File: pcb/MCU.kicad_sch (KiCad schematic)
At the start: 1 part, among them U1 WeMos_S2_mini

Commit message: added VR input IC conditioner
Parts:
- U1: footprint Module:WEMOS_S2_mini -> MCU_Custom:WEMOS_S2_mini
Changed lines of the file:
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@@
 			)
 		)
-		(property "Footprint" "Module:WEMOS_S2_mini"
+		(property "Footprint" "MCU_Custom:WEMOS_S2_mini"
 			(at 160.02 127 0)
 			(effects

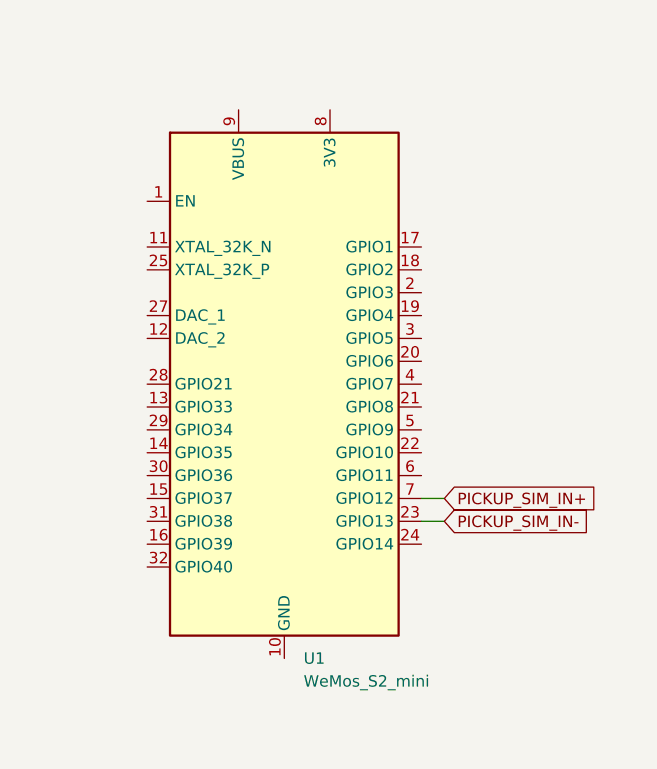
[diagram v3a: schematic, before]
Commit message: added SSR
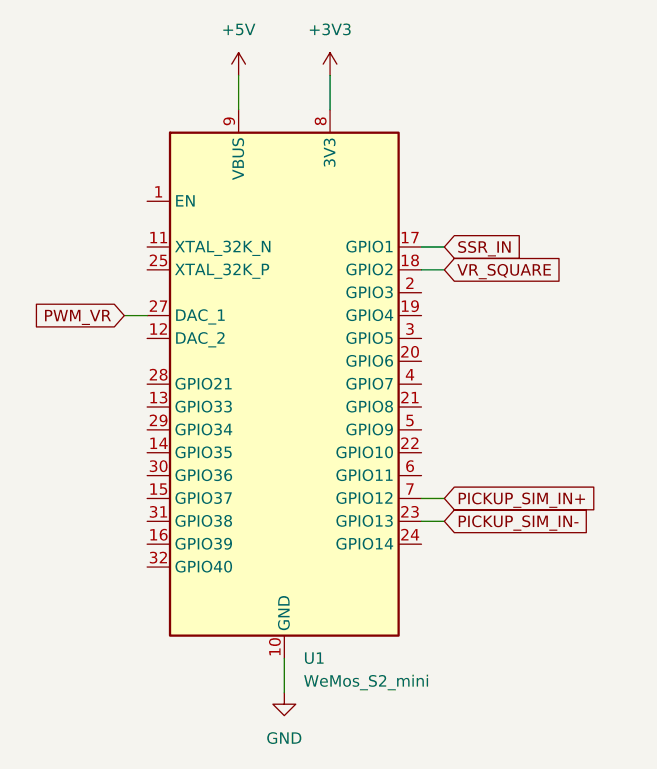
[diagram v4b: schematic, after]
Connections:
- net GND: now reaches U1.10 (GND), U1.26 (GND)
- net SSR_IN: now reaches U1.17 (GPIO1)
- net VR_SQUARE: now reaches U1.18 (GPIO2)
- net PWM_VR: now reaches U1.27 (DAC_1)
- net +3V3: now reaches U1.8 (3V3)
- net +5V: now reaches U1.9 (VBUS)

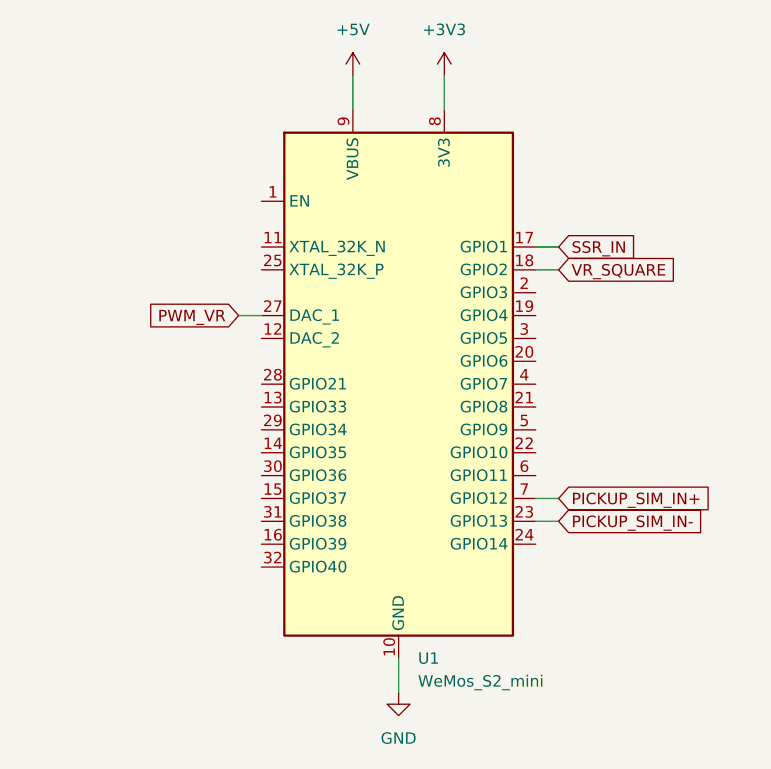
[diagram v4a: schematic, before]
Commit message: added batteryless function
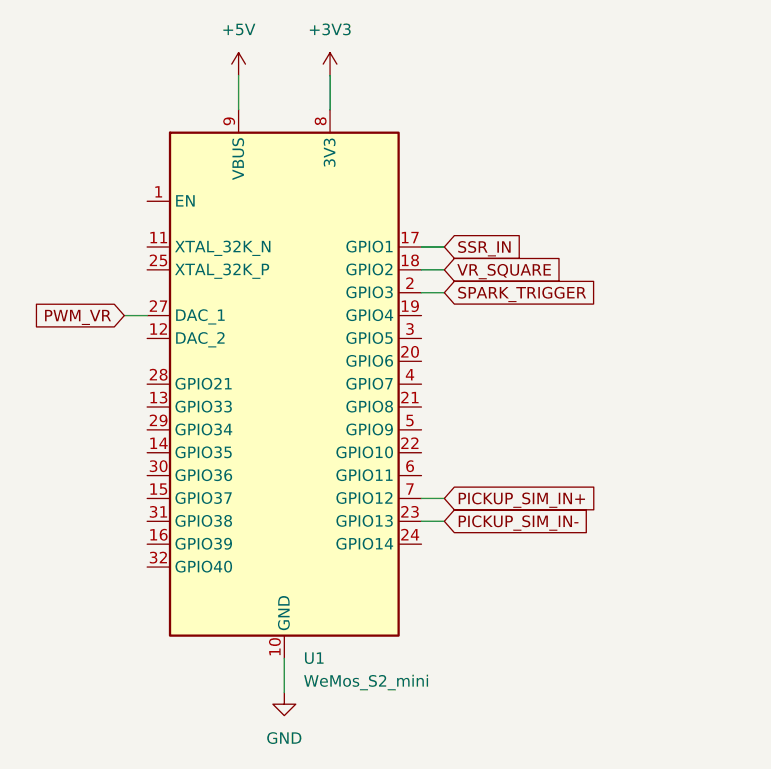
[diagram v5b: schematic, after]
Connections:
- net SPARK_TRIGGER: now reaches U1.2 (GPIO3)
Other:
- moved on the sheet: U1
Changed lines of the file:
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@@
 	(wire
 		(pts
-			(xy 154.94 46.99) (xy 154.94 50.8)
-		)
-		(stroke
-			(width 0)
-			(type default)
-		)
-	)
-	(wire
-		(pts
-			(xy 177.8 66.04) (xy 175.26 66.04)
-		)
-		(stroke
-			(width 0)
-			(type default)
-		)
-	)
-	(wire
-		(pts
-			(xy 160.02 115.57) (xy 160.02 111.76)
-		)
-		(stroke
-			(width 0)
-			(type default)
-		)
-	)
-	(wire
-		(pts
-			(xy 177.8 68.58) (xy 175.26 68.58)
-		)
-		(stroke
-			(width 0)
-			(type default)
-		)
-	)
-	(wire
-		(pts
-			(xy 165.1 46.99) (xy 165.1 50.8)
-		)
-		(stroke
-			(width 0)
-			(type default)
-		)
-	)
-	(wire
-		(pts
-			(xy 177.8 96.52) (xy 175.26 96.52)
-		)
-		(stroke
-			(width 0)
-			(type default)
-		)
-	)
-	(wire
-		(pts
-			(xy 177.8 93.98) (xy 175.26 93.98)
-		)
-		(stroke
-			(width 0)
-			(type default)
-		)
-	)
-	(wire
-		(pts
-			(xy 142.24 73.66) (xy 144.78 73.66)
-		)
-		(stroke
-			(width 0)
-			(type default)
-		)
-	)
-	(global_label "VR_SQUARE"
+			(xy 142.24 46.99) (xy 142.24 50.8)
+		)
+		(stroke
+			(width 0)
+			(type default)
+		)
+	)
+	(wire
+		(pts
+			(xy 165.1 71.12) (xy 162.56 71.12)
+		)
+		(stroke
+			(width 0)
+			(type default)
+		)
+	)
+	(wire
+		(pts
+			(xy 165.1 66.04) (xy 162.56 66.04)
+		)
+		(stroke
+			(width 0)
+			(type default)
+		)
+	)
+	(wire
+		(pts
+			(xy 147.32 115.57) (xy 147.32 111.76)
+		)
+		(stroke
+			(width 0)
+			(type default)
+		)
+	)
+	(wire
+		(pts
+			(xy 165.1 68.58) (xy 162.56 68.58)
+		)
+		(stroke
+			(width 0)
+			(type default)
+		)
+	)
+	(wire
+		(pts
+			(xy 152.4 46.99) (xy 152.4 50.8)
+		)
+		(stroke
+			(width 0)
+			(type default)
+		)
+	)
+	(wire
+		(pts
+			(xy 165.1 96.52) (xy 162.56 96.52)
+		)
+		(stroke
+			(width 0)
+			(type default)
+		)
+	)
+	(wire
+		(pts
+			(xy 165.1 93.98) (xy 162.56 93.98)
+		)
+		(stroke
+			(width 0)
+			(type default)
+		)
+	)
+	(wire
+		(pts
+			(xy 129.54 73.66) (xy 132.08 73.66)
+		)
+		(stroke
+			(width 0)
+			(type default)
+		)
+	)
+	(global_label "SPARK_TRIGGER"
 		(shape input)
-		(at 177.8 68.58 0)
+		(at 165.1 71.12 0)
 		(fields_autoplaced yes)
 		(effects
@@
 		)
 		(property "Intersheetrefs" "${INTERSHEET_REFS}"
-			(at 191.4895 68.58 0)
-			(effects
-				(font
-					(size 1.27 1.27)
-				)
-				(justify left)
-				(hide yes)
-			)
-		)
-	)
-	(global_label "PICKUP_SIM_IN+"
+			(at 182.9623 71.12 0)
+			(effects
+				(font
+					(size 1.27 1.27)
+				)
+				(justify left)
+				(hide yes)
+			)
+		)
+	)
+	(global_label "VR_SQUARE"
 		(shape input)
-		(at 177.8 93.98 0)
+		(at 165.1 68.58 0)
 		(fields_autoplaced yes)
 		(effects
@@
 		)
 		(property "Intersheetrefs" "${INTERSHEET_REFS}"
-			(at 196.5091 93.98 0)
-			(effects
-				(font
-					(size 1.27 1.27)
-				)
-				(justify left)
-				(hide yes)
-			)
-		)
-	)
-	(global_label "PICKUP_SIM_IN-"
+			(at 178.7895 68.58 0)
+			(effects
+				(font
+					(size 1.27 1.27)
+				)
+				(justify left)
+				(hide yes)
+			)
+		)
+	)
+	(global_label "PICKUP_SIM_IN+"
 		(shape input)
-		(at 177.8 96.52 0)
+		(at 165.1 93.98 0)
 		(fields_autoplaced yes)
 		(effects
@@
 		)
 		(property "Intersheetrefs" "${INTERSHEET_REFS}"
-			(at 196.5091 96.52 0)
-			(effects
-				(font
-					(size 1.27 1.27)
-				)
-				(justify left)
-				(hide yes)
-			)
-		)
-	)
-	(global_label "SSR_IN"
+			(at 183.8091 93.98 0)
+			(effects
+				(font
+					(size 1.27 1.27)
+				)
+				(justify left)
+				(hide yes)
+			)
+		)
+	)
+	(global_label "PICKUP_SIM_IN-"
 		(shape input)
-		(at 177.8 66.04 0)
+		(at 165.1 96.52 0)
 		(fields_autoplaced yes)
 		(effects
@@
 		)
 		(property "Intersheetrefs" "${INTERSHEET_REFS}"
-			(at 187.3771 66.04 0)
-			(effects
-				(font
-					(size 1.27 1.27)
-				)
-				(justify left)
-				(hide yes)
-			)
-		)
-	)
-	(global_label "PWM_VR"
+			(at 183.8091 96.52 0)
+			(effects
+				(font
+					(size 1.27 1.27)
+				)
+				(justify left)
+				(hide yes)
+			)
+		)
+	)
+	(global_label "SSR_IN"
 		(shape input)
-		(at 142.24 73.66 180)
+		(at 165.1 66.04 0)
 		(fields_autoplaced yes)
 		(effects
@@
 				(size 1.27 1.27)
 			)
+			(justify left)
+		)
+		(property "Intersheetrefs" "${INTERSHEET_REFS}"
+			(at 174.6771 66.04 0)
+			(effects
+				(font
+					(size 1.27 1.27)
+				)
+				(justify left)
+				(hide yes)
+			)
+		)
+	)
+	(global_label "PWM_VR"
+		(shape input)
+		(at 129.54 73.66 180)
+		(fields_autoplaced yes)
+		(effects
+			(font
+				(size 1.27 1.27)
+			)
 			(justify right)
 		)
 		(property "Intersheetrefs" "${INTERSHEET_REFS}"
-			(at 131.7558 73.66 0)
+			(at 119.0558 73.66 0)
 			(effects
 				(font
@@
 	(symbol
 		(lib_id "power:+5V")
-		(at 154.94 46.99 0)
+		(at 142.24 46.99 0)
 		(unit 1)
 		(exclude_from_sim no)
@@
 		(fields_autoplaced yes)
 		(property "Reference" "#PWR08"
-			(at 154.94 50.8 0)
+			(at 142.24 50.8 0)
 			(effects
 				(font
@@
 		)
 		(property "Value" "+5V"
-			(at 154.94 41.91 0)
+			(at 142.24 41.91 0)
 			(effects
 				(font
@@
 		)
 		(property "Footprint" ""
-			(at 154.94 46.99 0)
+			(at 142.24 46.99 0)
 			(effects
 				(font
@@
 		)
 		(property "Datasheet" ""
-			(at 154.94 46.99 0)
+			(at 142.24 46.99 0)
 			(effects
 				(font
@@
 		)
 		(property "Description" "Power symbol creates a global label with name \"+5V\""
-			(at 154.94 46.99 0)
+			(at 142.24 46.99 0)
 			(effects
 				(font
@@
 	(symbol
 		(lib_id "power:+3V3")
-		(at 165.1 46.99 0)
+		(at 152.4 46.99 0)
 		(unit 1)
 		(exclude_from_sim no)
@@
 		(fields_autoplaced yes)
 		(property "Reference" "#PWR07"
-			(at 165.1 50.8 0)
+			(at 152.4 50.8 0)
 			(effects
 				(font
@@
 		)
 		(property "Value" "+3V3"
-			(at 165.1 41.91 0)
+			(at 152.4 41.91 0)
 			(effects
 				(font
@@
 		)
 		(property "Footprint" ""
-			(at 165.1 46.99 0)
+			(at 152.4 46.99 0)
 			(effects
 				(font
@@
 		)
 		(property "Datasheet" ""
-			(at 165.1 46.99 0)
+			(at 152.4 46.99 0)
 			(effects
 				(font
@@
 		)
 		(property "Description" "Power symbol creates a global label with name \"+3V3\""
-			(at 165.1 46.99 0)
+			(at 152.4 46.99 0)
 			(effects
 				(font
@@
 	(symbol
 		(lib_id "MCU_Custom:WeMos_S2_mini")
-		(at 160.02 81.28 0)
+		(at 147.32 81.28 0)
 		(unit 1)
 		(exclude_from_sim no)
@@
 		(fields_autoplaced yes)
 		(property "Reference" "U1"
-			(at 162.1633 111.76 0)
+			(at 149.4633 111.76 0)
 			(effects
 				(font
@@
 		)
 		(property "Value" "WeMos_S2_mini"
-			(at 162.1633 114.3 0)
+			(at 149.4633 114.3 0)
 			(effects
 				(font
@@
 		)
 		(property "Footprint" "MCU_Custom:WEMOS_S2_mini"
-			(at 160.02 127 0)
+			(at 147.32 127 0)
 			(effects
 				(font
@@
 		)
 		(property "Datasheet" "https://www.wemos.cc/en/latest/s2/s2_mini.html"
-			(at 160.02 124.46 0)
+			(at 147.32 124.46 0)
 			(effects
 				(font
@@
 		)
 		(property "Description" "32-bit microcontroller module with WiFi"
-			(at 160.02 81.28 0)
+			(at 147.32 81.28 0)
 			(effects
 				(font
@@
 	(symbol
 		(lib_id "power:GND")
-		(at 160.02 115.57 0)
+		(at 147.32 115.57 0)
 		(unit 1)
 		(exclude_from_sim no)
@@
 		(fields_autoplaced yes)
 		(property "Reference" "#PWR06"
-			(at 160.02 121.92 0)
+			(at 147.32 121.92 0)
 			(effects
 				(font
@@
 		)
 		(property "Value" "GND"
-			(at 160.02 120.65 0)
+			(at 147.32 120.65 0)
 			(effects
 				(font
@@
 		)
 		(property "Footprint" ""
-			(at 160.02 115.57 0)
+			(at 147.32 115.57 0)
 			(effects
 				(font
@@
 		)
 		(property "Datasheet" ""
-			(at 160.02 115.57 0)
+			(at 147.32 115.57 0)
 			(effects
 				(font
@@
 		)
 		(property "Description" "Power symbol creates a global label with name \"GND\" , ground"
-			(at 160.02 115.57 0)
-			(effects
-				(font
+			(at 147.32 115.57 0)
+			(effects
+				(font

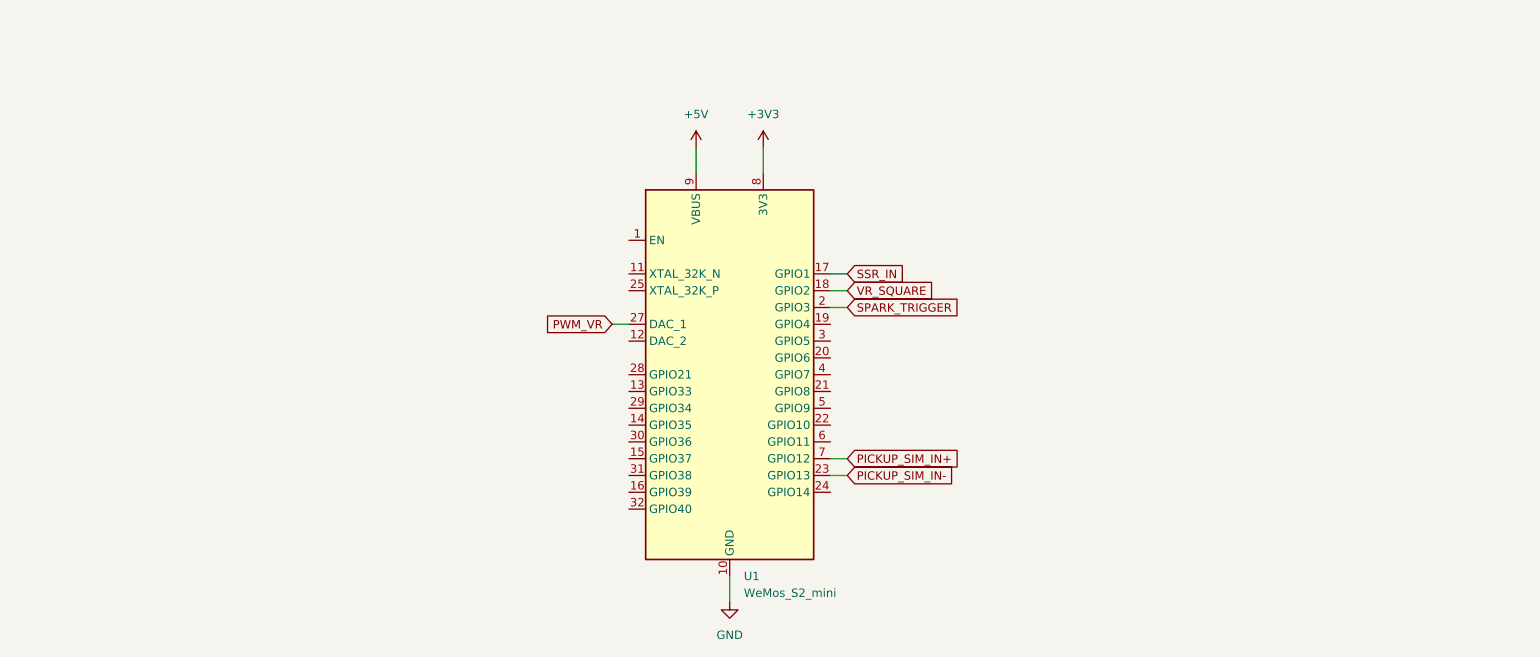
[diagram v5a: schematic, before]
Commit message: added SCR from kill switch to GND and RGB led
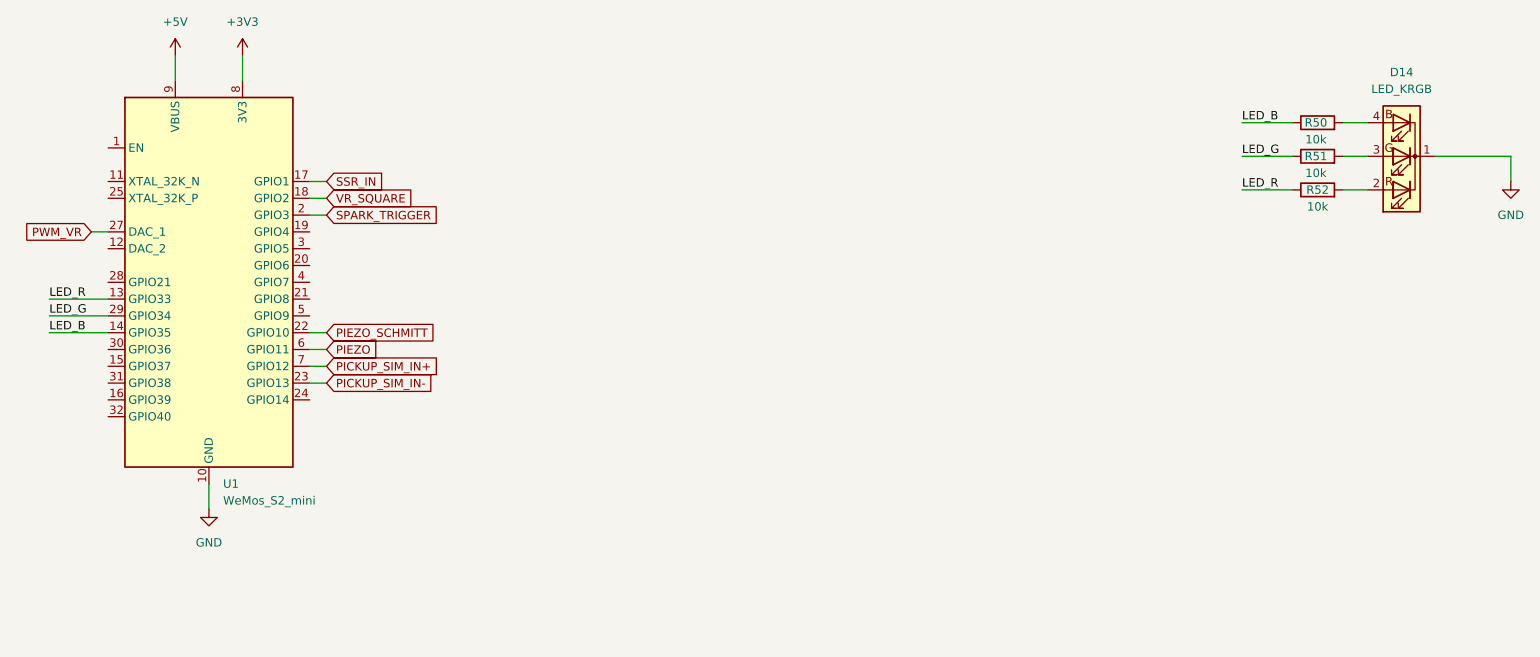
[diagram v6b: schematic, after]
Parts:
- added D14: LED_KRGB, symbol Device:LED_KRGB
- added R50, R51, R52: 10k, Resistor_SMD:R_0201_0603Metric, symbol Device:R
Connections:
- net GND: now also D14.1 (K)
- net LED_R: now reaches U1.13 (GPIO33)
- net LED_R: now also R52.1
- net LED_B: now reaches U1.14 (GPIO35)
- net LED_B: now also R50.1
- net PIEZO_SCHMITT: now reaches U1.22 (GPIO10)
- net LED_G: now reaches U1.29 (GPIO34)
- net LED_G: now also R51.1
- net PIEZO: now reaches U1.6 (GPIO11)
- new net: D14.2 (RA), R52.2
- new net: D14.3 (GA), R51.2
- new net: D14.4 (BA), R50.2
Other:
- moved on the sheet: U1

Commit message: added digital input for QS
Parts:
- D14: footprint (none) -> LED_THT:LED_D5.0mm-4_RGB_Wide_Pins
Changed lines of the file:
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@@
 			)
 		)
-		(property "Footprint" ""
+		(property "Footprint" "LED_THT:LED_D5.0mm-4_RGB_Wide_Pins"
 			(at 248.92 46.99 0)
 			(effects

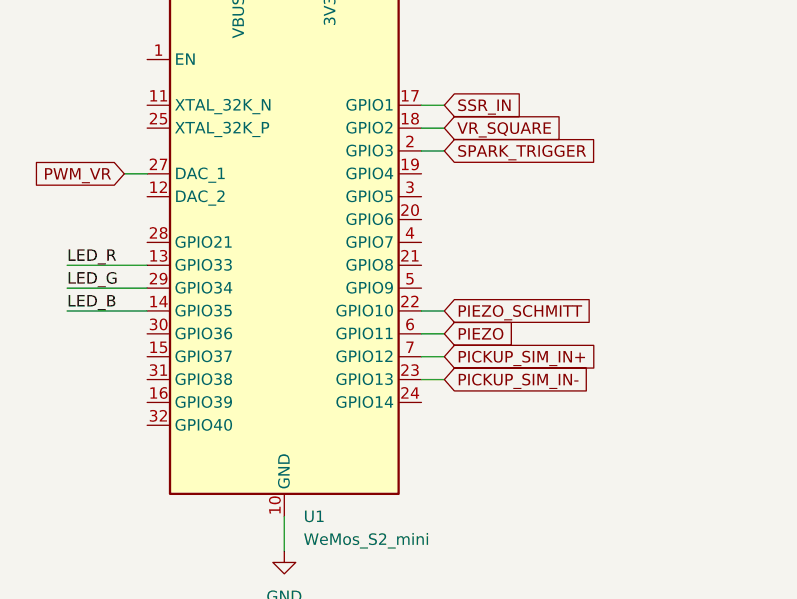
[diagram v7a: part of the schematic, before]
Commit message: fixed basic pcb errors
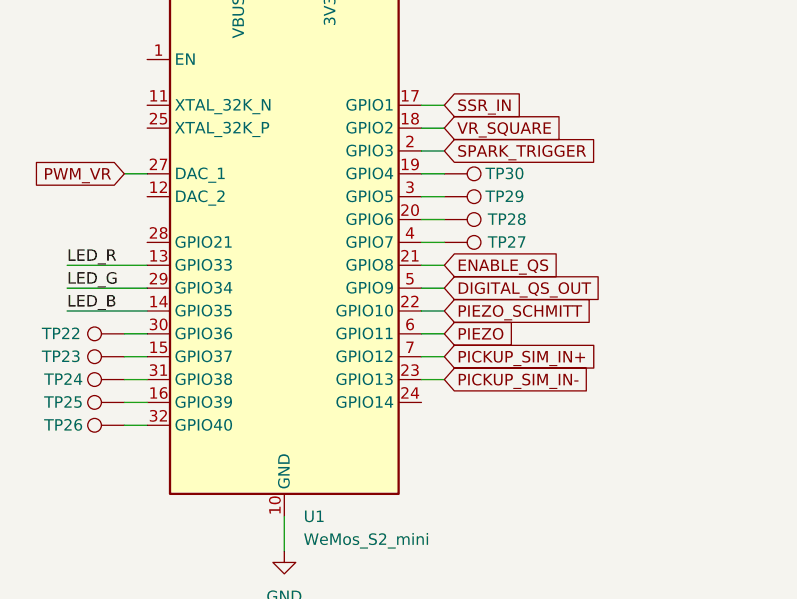
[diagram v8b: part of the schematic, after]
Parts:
- added TP22, TP23, TP24, TP25, TP26, TP27, TP28, TP29, TP30: TestPoint, Connector_PinHeader_1.00mm:PinHeader_1x01_P1.00mm_Vertical, symbol Connector:TestPoint
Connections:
- net at U1.15 (GPIO37): now also TP23.1
- net at U1.16 (GPIO39): now also TP25.1
- net at U1.19 (GPIO4): now also TP30.1
- net at U1.20 (GPIO6): now also TP28.1
- net ENABLE_QS: now reaches U1.21 (GPIO8)
- net at U1.3 (GPIO5): now also TP29.1
- net at U1.30 (GPIO36): now also TP22.1
- net at U1.31 (GPIO38): now also TP24.1
- net at U1.32 (GPIO40): now also TP26.1
- net at U1.4 (GPIO7): now also TP27.1
- net DIGITAL_QS_OUT: now reaches U1.5 (GPIO9)
